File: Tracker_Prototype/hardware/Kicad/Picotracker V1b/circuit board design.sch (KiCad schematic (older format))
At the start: 55 parts, among them IC7 SPV1040, J1 Conn_01x06, J2 GND, J3 +SOL, J4 BATT_V+, J5 BATT_GND, J6 ICSS LOGO, Q1 Q_PMOS_DGS, SW1 SW_Push, U2 TPS62740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

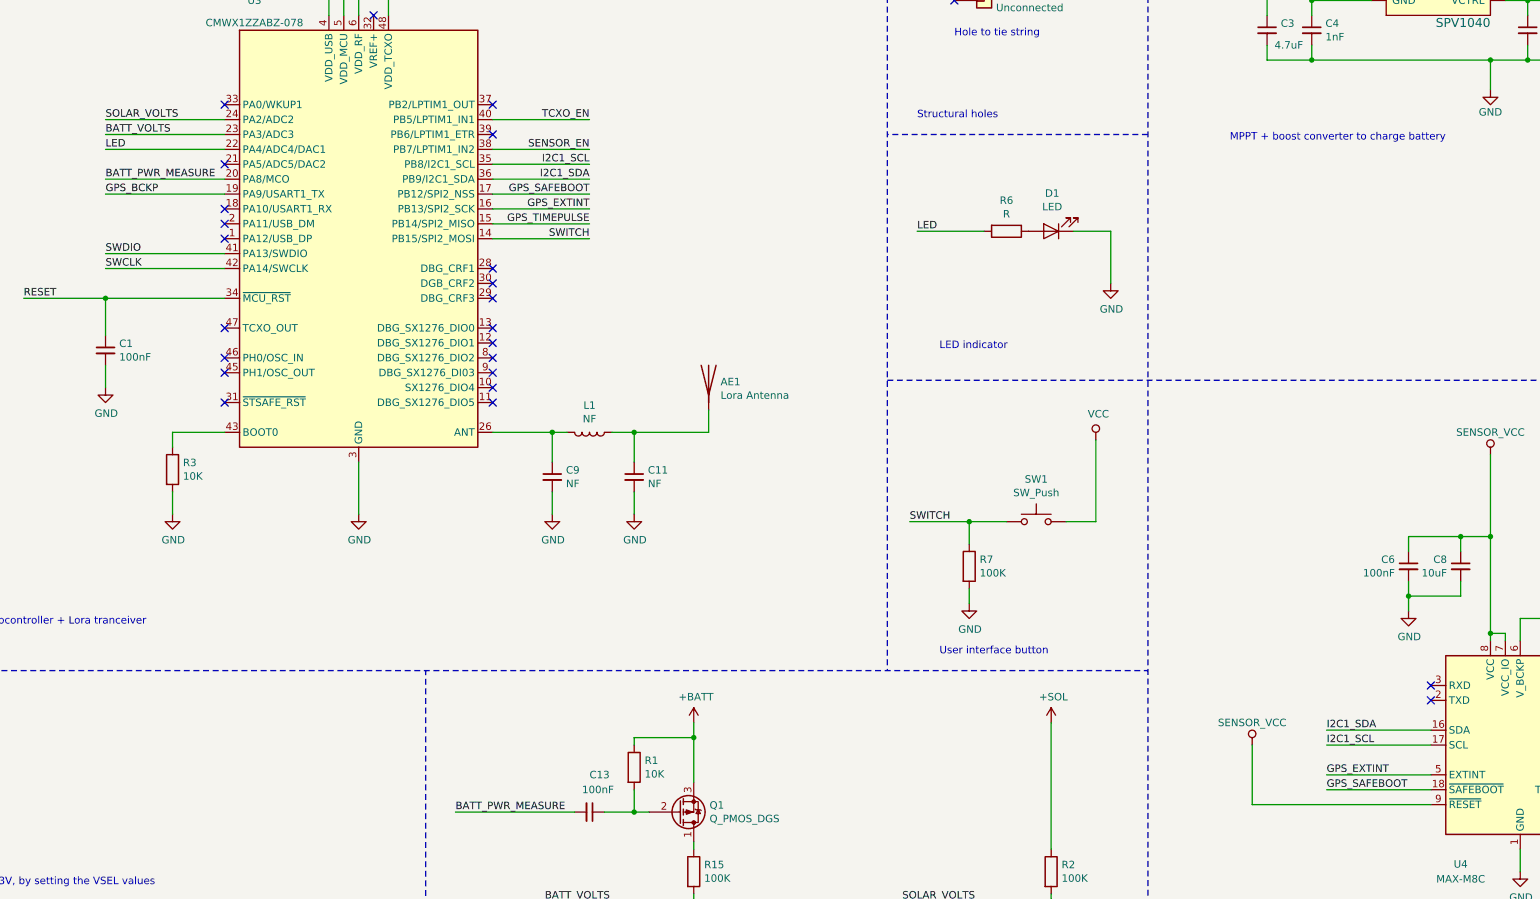
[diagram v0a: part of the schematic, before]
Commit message: Routed most of the swaped config board
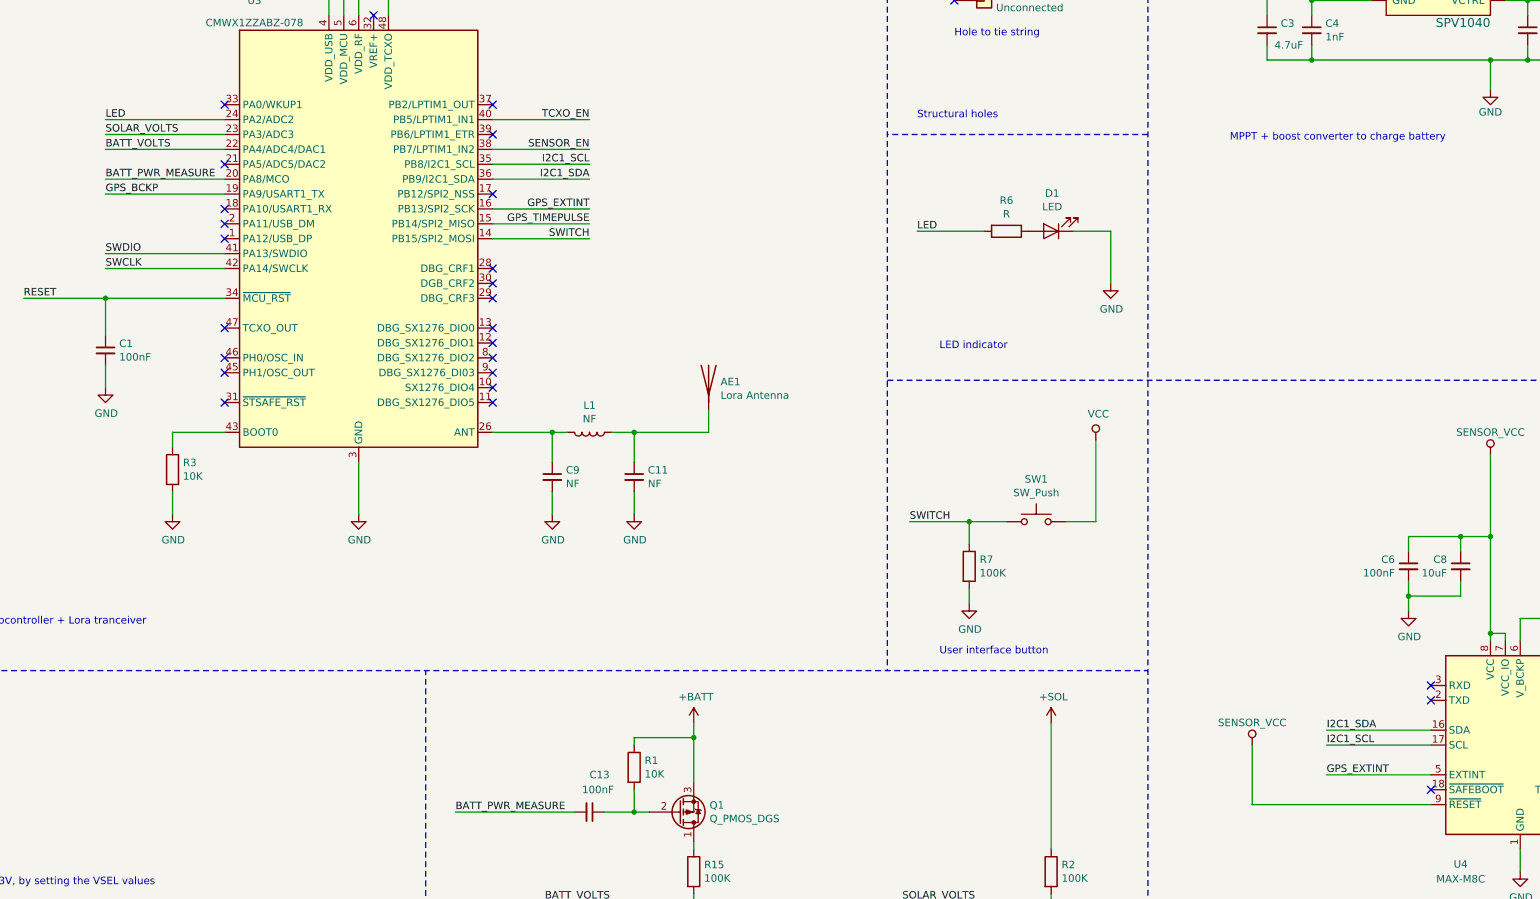
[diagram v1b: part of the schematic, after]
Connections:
- net BATT_VOLTS: now also U3.22 (PA4/ADC4/DAC1); no longer U3.23 (PA3/ADC3)
- net LED: now also U3.24 (PA2/ADC2); no longer U3.22 (PA4/ADC4/DAC1)
- net SOLAR_VOLTS: now also U3.23 (PA3/ADC3); no longer U3.24 (PA2/ADC2)
- net GPS_SAFEBOOT: no longer names the net of U4.18 (~SAFEBOOT)
- net GPS_SAFEBOOT: no longer U3.17 (PB12/SPI2_NSS)
- no-connect marks 31 -> 33
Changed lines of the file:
@@
 Structural plated throughole to \nhold the guitar wire solar \ncell structure
 Wire Wire Line
-	4900 3150 4100 3150
+	4900 3250 4100 3250
 Wire Wire Line
 	4300 1400 5600 1400
@@
 NoConn ~ 4900 3950
 Wire Wire Line
-	4900 3350 4100 3350
+	4900 3150 4100 3150
 Wire Wire Line
 	10850 3900 10850 4250
@@
 Wire Notes Line
 	9350 650  9350 6850
-Text Label 4100 3350 0    50   ~ 0
+Text Label 4100 3150 0    50   ~ 0
 LED
 Text Label 9550 3900 0    50   ~ 0
@@
 Wire Wire Line
 	11800 7750 11800 7350
-Text Label 12300 7650 0    50   ~ 0
-GPS_SAFEBOOT
 Text Label 12300 7550 0    50   ~ 0
 GPS_EXTINT
-Wire Wire Line
-	13000 7750 11800 7750
 Wire Wire Line
 	13400 6600 13400 6650
@@
 NoConn ~ 13000 6950
 NoConn ~ 13000 7050
-Wire Wire Line
-	13000 7650 12300 7650
 Wire Wire Line
 	12300 7350 13000 7350
@@
 Text Label 7350 3850 2    50   ~ 0
 GPS_TIMEPULSE
-Text Label 7350 3650 2    50   ~ 0
-GPS_SAFEBOOT
 Wire Wire Line
 	6700 3750 7350 3750
-Wire Wire Line
-	6700 3650 7350 3650
 Wire Wire Line
 	6700 3550 7350 3550
@@
 	1    0    0    -1
 $EndComp
-Text Label 4100 3150 0    50   ~ 0
+Text Label 4100 3250 0    50   ~ 0
 SOLAR_VOLTS
 Wire Wire Line
-	4900 3250 4100 3250
-Text Label 4100 3250 0    50   ~ 0
+	4900 3350 4100 3350
+Text Label 4100 3350 0    50   ~ 0
 BATT_VOLTS
 Text Label 4100 3550 0    50   ~ 0
@@
 	1    0    0    -1
 $EndComp
+Wire Wire Line
+	13000 7750 11800 7750
+NoConn ~ 13000 7650
+NoConn ~ 6700 3650
 $EndSCHEMATC

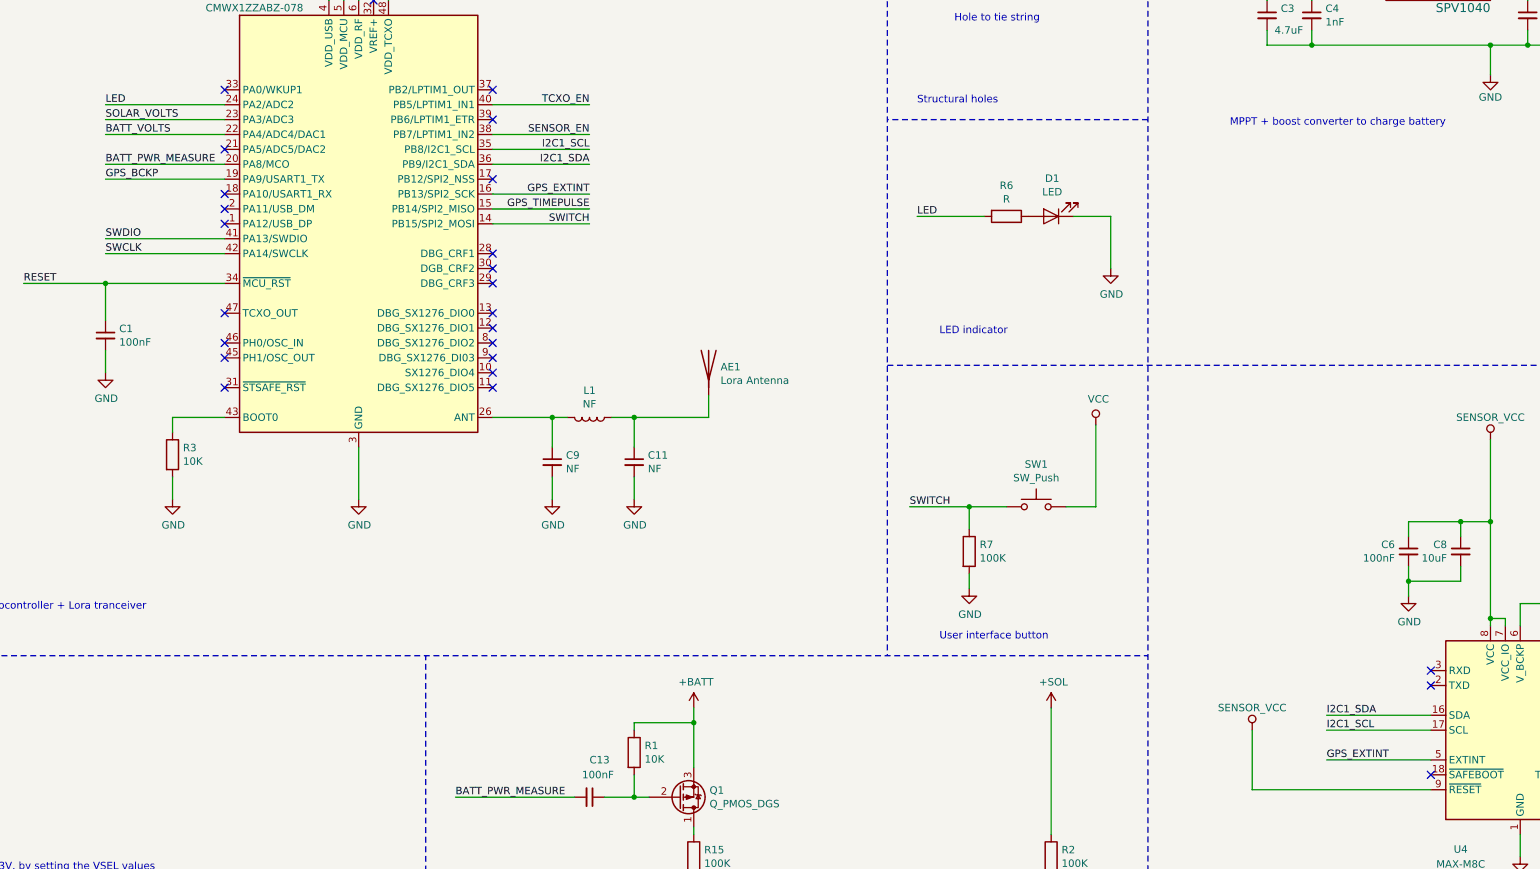
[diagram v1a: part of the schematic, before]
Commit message: Finished the layout of both the a and b variants. Silkscreen also done
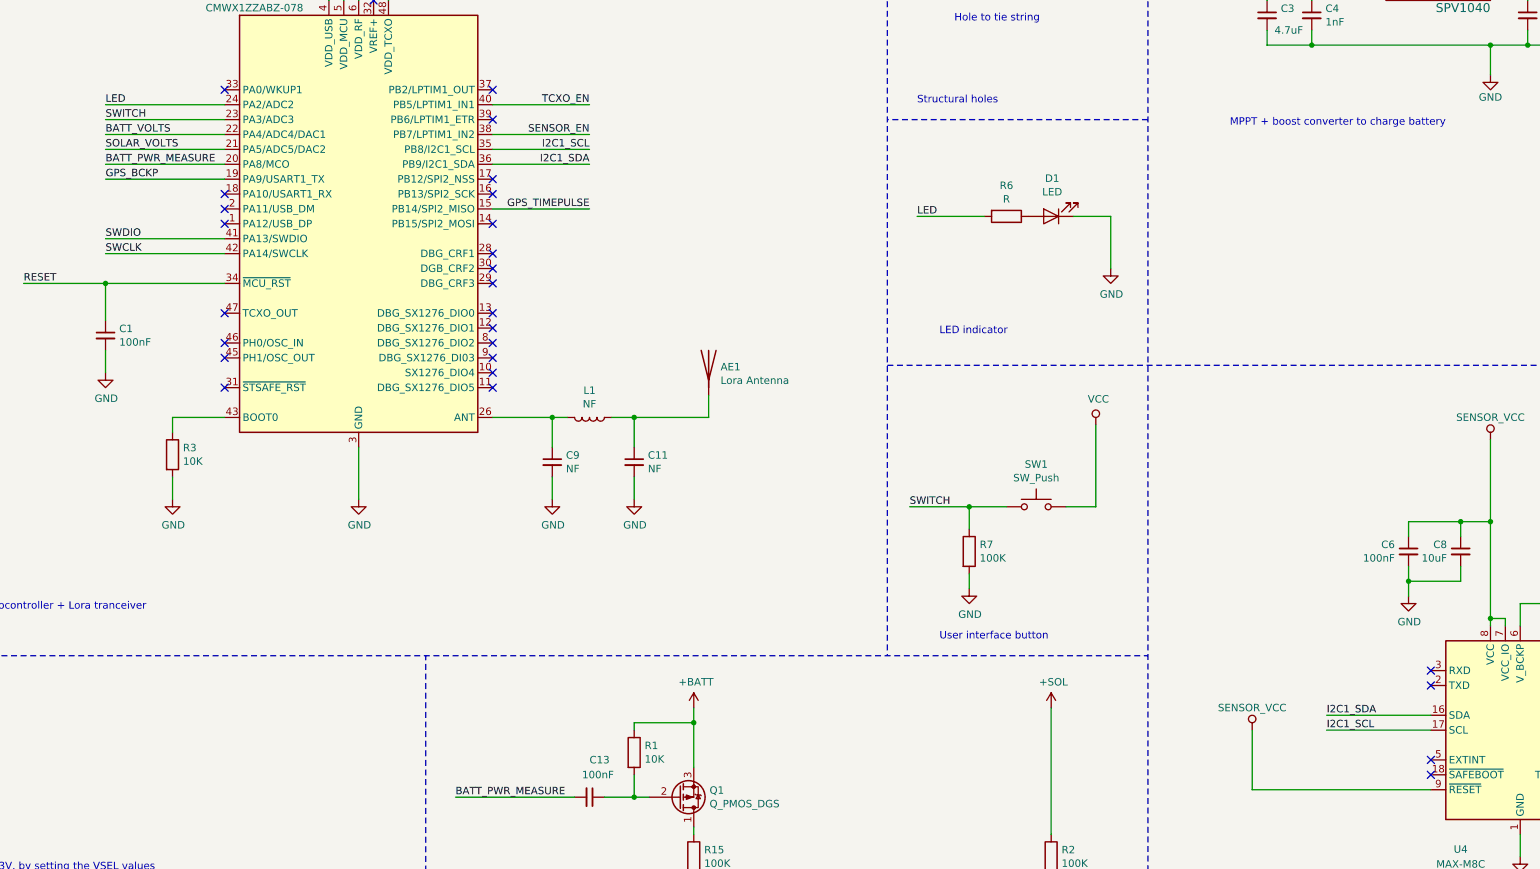
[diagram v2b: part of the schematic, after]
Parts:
- L2, L3: footprint Inductor_SMD:L_Taiyo-Yuden_NR-30xx -> flight-computer:L_Coilcraft_LPS3015
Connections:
- net SOLAR_VOLTS: now also U3.21 (PA5/ADC5/DAC2); no longer U3.23 (PA3/ADC3)
- net SWITCH: now also U3.23 (PA3/ADC3); no longer U3.14 (PB15/SPI2_MOSI)
- net GPS_EXTINT: no longer names the net of U4.5 (EXTINT)
- net GPS_EXTINT: no longer U3.16 (PB13/SPI2_SCK)
- no-connect marks 33 -> 35
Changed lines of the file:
@@
 NoConn ~ 6700 4950
 NoConn ~ 6700 5050
-NoConn ~ 4900 3450
 NoConn ~ 4900 3050
 NoConn ~ 4900 4850
@@
 Structural plated throughole to \nhold the guitar wire solar \ncell structure
 Wire Wire Line
-	4900 3250 4100 3250
+	4900 3450 4100 3450
 Wire Wire Line
 	4300 1400 5600 1400
@@
 Wire Wire Line
 	11800 7750 11800 7350
-Text Label 12300 7550 0    50   ~ 0
-GPS_EXTINT
 Wire Wire Line
 	13400 6600 13400 6650
 Wire Wire Line
 	13500 6650 13500 6600
-Wire Wire Line
-	13000 7550 12300 7550
 NoConn ~ 13000 6950
 NoConn ~ 13000 7050
@@
 Text Label 7350 3550 2    50   ~ 0
 I2C1_SDA
-Text Label 7350 3750 2    50   ~ 0
-GPS_EXTINT
-Wire Wire Line
-	6700 3850 7350 3850
-Wire Wire Line
-	6700 3950 7350 3950
-Text Label 7350 3950 2    50   ~ 0
+Wire Wire Line
+	4900 3250 4100 3250
+Text Label 4100 3250 0    50   ~ 0
 SWITCH
-Text Label 7350 3850 2    50   ~ 0
-GPS_TIMEPULSE
-Wire Wire Line
-	6700 3750 7350 3750
 Wire Wire Line
 	6700 3550 7350 3550
@@
 F 0 "L2" V 4019 8950 50  0000 C CNN
 F 1 "2.2uH" V 4110 8950 50  0000 C CNN
-F 2 "Inductor_SMD:L_Taiyo-Yuden_NR-30xx" H 4200 8950 50  0001 C CNN
+F 2 "flight-computer:L_Coilcraft_LPS3015" H 4200 8950 50  0001 C CNN
 F 3 "~" H 4200 8950 50  0001 C CNN
 	1    4200 8950
@@
 F 0 "L3" V 12269 1850 50  0000 C CNN
 F 1 "10uH" V 12360 1850 50  0000 C CNN
-F 2 "Inductor_SMD:L_Taiyo-Yuden_NR-30xx" H 12450 1850 50  0001 C CNN
+F 2 "flight-computer:L_Coilcraft_LPS3015" H 12450 1850 50  0001 C CNN
 F 3 "https://www.mouser.co.uk/datasheet/2/597/lps3015-270734.pdf" H 12450 1850 50  0001 C CNN
 	1    12450 1850
@@
 	1    0    0    -1
 $EndComp
-Text Label 4100 3250 0    50   ~ 0
+Text Label 4100 3450 0    50   ~ 0
 SOLAR_VOLTS
 Wire Wire Line
@@
 	1    0    0    -1
 $EndComp
-Wire Wire Line
-	13000 7750 11800 7750
 NoConn ~ 13000 7650
 NoConn ~ 6700 3650
+NoConn ~ 6700 3950
+Wire Wire Line
+	13000 7750 11800 7750
+NoConn ~ 13000 7550
+Text Label 7350 3850 2    50   ~ 0
+GPS_TIMEPULSE
+Wire Wire Line
+	6700 3850 7350 3850
+NoConn ~ 6700 3750
 $EndSCHEMATC

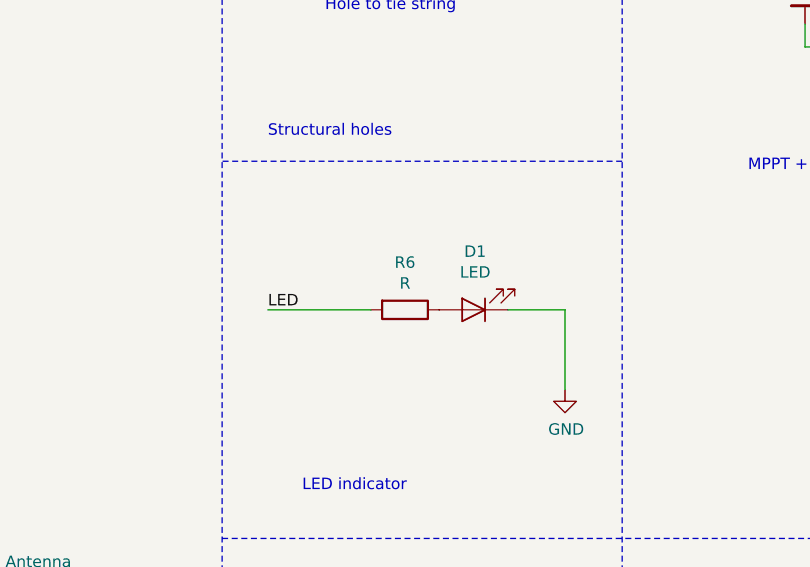
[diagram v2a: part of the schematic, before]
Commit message: updated the bom with links to purchase. got the interactive bom to work
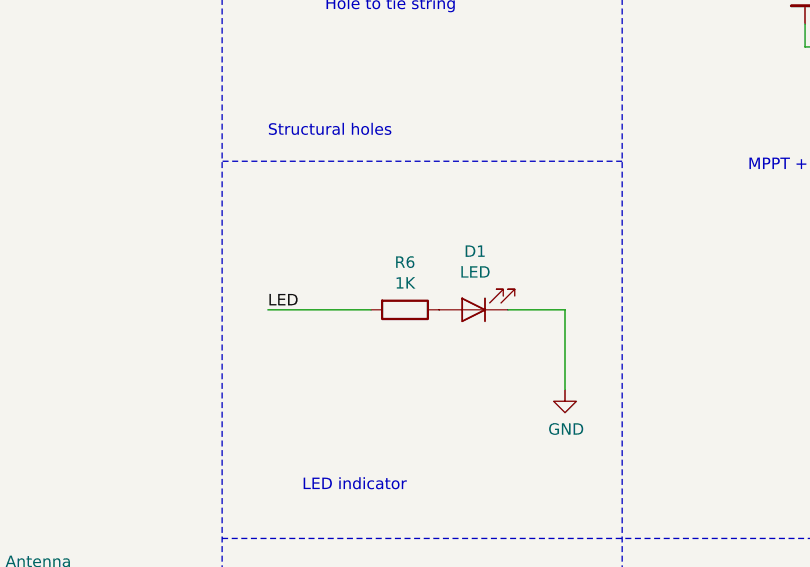
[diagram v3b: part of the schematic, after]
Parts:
- C1, C13, C5: Cost (none) -> 0.017; Purchase link (none) -> https://uk.rs-online.com/web/p/mlccs-multilayer-ceramic-cap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; min_quantity (none) -> 100
- C10, C12, C2: Purchase link (none) -> https://uk.rs-online.com/web/p/mlccs-multilayer-ceramic-cap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; min_quantity (none) -> 100
- C16, C4: Cost (none) -> 0.011; Purchase link (none) -> https://uk.rs-online.com/web/p/mlccs-multilayer-ceramic-cap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; min_quantity (none) -> 100
- C17: Cost (none) -> 0.0107; Purchase link (none) -> https://uk.rs-online.com/web/p/mlccs-multilayer-ceramic-cap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; min_quantity (none) -> 10
- C3: Cost (none) -> 0.074; Purchase link (none) -> https://uk.rs-online.com/web/p/mlccs-multilayer-ceramic-cap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; min_quantity (none) -> 50
- C6: Cost 0.01 -> 0.017; Purchase link https://uk.rs-online.com/web/p/mlccs-multilayer-ceramic-capacitors/6983251/ -> https://uk.rs-online.com/web/p/mlccs-multilayer-ceramic-capacitors/6983207/; min_quantity 50 -> 100
- D1: Cost (none) -> 0.155; Purchase link (none) -> https://uk.rs-online.com/web/p/leds/4663649/; min_quantity (none) -> 20
- D2: Cost (none) -> 0.22; min_quantity (none) -> 25
- IC7: Cost (none) -> 2.95; Purchase link (none) -> https://uk.farnell.com/stmicroelectronics/spv1040t/battery-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; min_quantity (none) -> 1
- L2: Cost (none) -> 1.41; Purchase link (none) -> https://uk.farnell.com/coilcraft/lps3015-222mrb/inductor-2-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; min_quantity (none) -> 1
- L3: Cost (none) -> 1.42; Purchase link (none) -> https://uk.farnell.com/coilcraft/lps3015-103mrb/inductor-10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; min_quantity (none) -> 1
- Q1: Cost (none) -> 0.415; Purchase link (none) -> https://uk.rs-online.com/web/p/mosfets/0301322/; min_quantity (none) -> 5
- R1, R3: Cost (none) -> 0.033; Purchase link (none) -> https://uk.rs-online.com/web/p/surface-mount-fixed-resistor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; min_quantity (none) -> 50
- R10, R11, R8: Cost (none) -> 0.0114; Purchase link (none) -> https://uk.farnell.com/vishay/crcw04021k00fked/res-1k-1-0-0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; min_quantity (none) -> 150
- R12: Cost (none) -> 0.0004; Purchase link (none) -> https://uk.rs-online.com/web/p/surface-mount-fixed-resistor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; min_quantity (none) -> 100
- R13: Cost (none) -> 0.02; Purchase link (none) -> https://uk.rs-online.com/web/p/surface-mount-fixed-resistor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; min_quantity (none) -> 50
- R14: Cost (none) -> 0.0137; Purchase link (none) -> https://uk.farnell.com/yageo/rc0402fr-075m1l/res-5m1-1-0-06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; min_quantity (none) -> 10
- R15, R16, R2, R7, R9: Cost (none) -> 0.0114; Purchase link (none) -> https://uk.farnell.com/vishay/crcw0402100kfked/res-100k-1-0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; min_quantity (none) -> 150
- R4, R5: Cost 0.01 -> 0.0002; Purchase link https://uk.rs-online.com/web/p/surface-mount-fixed-resistors/7408877/ -> https://uk.rs-online.com/web/p/surface-mount-fixed-resistors/3715086/
- R6: value R -> 1K; Cost (none) -> 0.0114; Purchase link (none) -> https://uk.farnell.com/vishay/crcw04021k00fked/res-1k-1-0-0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; min_quantity (none) -> 150
- SW1: Cost (none) -> 0.207; Purchase link (none) -> https://uk.rs-online.com/web/p/tactile-switches/1250189/?re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; min_quantity (none) -> 10
- U2: Cost (none) -> 1.575; Purchase link (none) -> https://uk.rs-online.com/web/p/buck-converters/8257018/; min_quantity (none) -> 2
- U3: Cost (none) -> 13.32; Purchase link (none) -> https://uk.rs-online.com/web/p/radio-frequency-development-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; min_quantity (none) -> 1
